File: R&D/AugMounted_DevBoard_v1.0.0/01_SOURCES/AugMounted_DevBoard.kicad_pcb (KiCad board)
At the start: 4 copper layers, 55.1 x 83.3 mm, 136 parts, among them J201 J_TYPE-C-31-M-13, J301 J_JST_S2B-PH-SM4-TB, J401 J_FH43BW-61S-0.2SHW, J501 J_0788641001_PAD, J504 J_0788641001_PAD, Q301 Q_BSS123WQ-7-F, Q302 Q_HSS2P10, Q303 Q_BSS123WQ-7-F, Q304 Q_HSS2P10, Q305 Q_BSS123WQ-7-F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

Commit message: Layout done
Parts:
- moved LOGO101 13.4 mm to (164.6, 75.9), turned to 180 degrees
- moved JP403 0.15 mm to (152.5, 114.2)
- moved JP401 0.15 mm to (157.5, 114.2)
- moved JP402 0.15 mm to (155.0, 114.2)
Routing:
- net GND: vias 104 -> 174

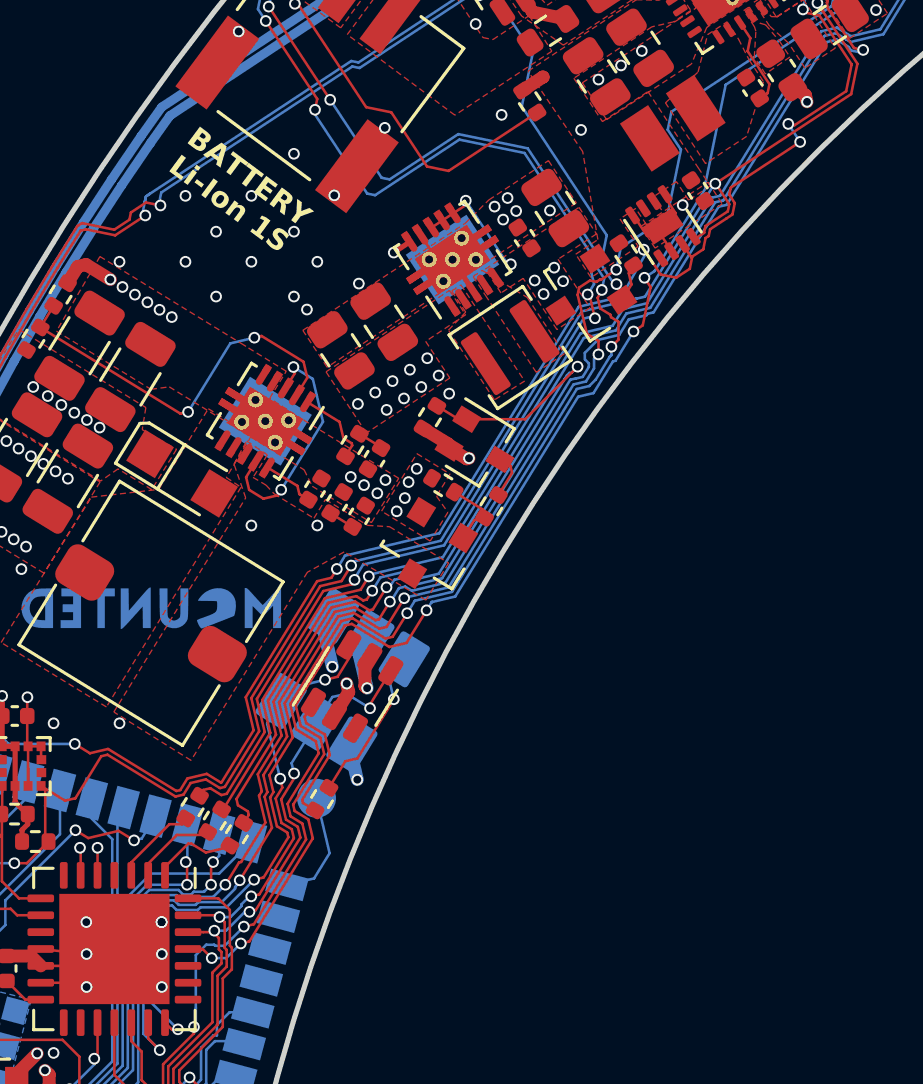
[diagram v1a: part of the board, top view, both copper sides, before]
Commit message: Excluded violations, added via stiching for GND. Ready for review/Production
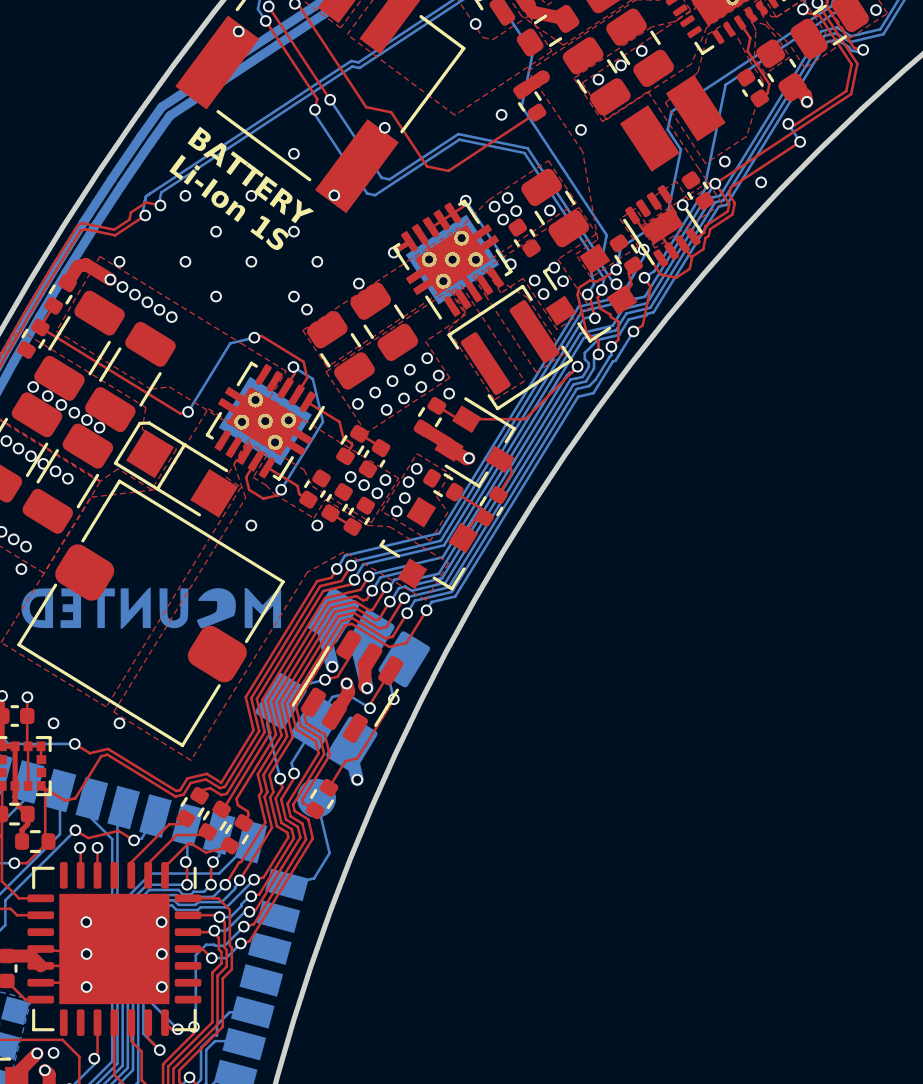
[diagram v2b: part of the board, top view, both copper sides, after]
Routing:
- net GND: vias 174 -> 175
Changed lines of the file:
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@@
           (xy 179.603773 41.320426)
           (xy 178.150624 42.694601)
-          (xy 177.326118 41.822712)
+          (xy 177.326119 41.822712)
           (xy 178.779268 40.448536)
         )
@@
           (xy 179.603773 41.320426)
           (xy 178.150624 42.694601)
-          (xy 177.326118 41.822712)
+          (xy 177.326119 41.822712)
           (xy 178.779268 40.448536)
         )
@@
   (via (at 157.160398 91.518971) (size 0.45) (drill 0.3) (layers "F.Cu" "B.Cu") (free) (net 1))
   (via (at 172.643827 63.36587) (size 0.45) (drill 0.3) (layers "F.Cu" "B.Cu") (free) (net 1))
-  (via (at 165.043827 87.96587) (size 0.45) (drill 0.3) (layers "F.Cu" "B.Cu") (net 1))
   (via (at 158.951135 108.343453) (size 0.45) (drill 0.3) (layers "F.Cu" "B.Cu") (net 1))
   (via (at 194.643827 52.86587) (size 0.45) (drill 0.3) (layers "F.Cu" "B.Cu") (free) (net 1))
@@
   (via (at 188.633169 45.090277) (size 0.45) (drill 0.3) (layers "F.Cu" "B.Cu") (net 1))
   (via (at 186.935187 43.779551) (size 0.45) (drill 0.3) (layers "F.Cu" "B.Cu") (net 1))
+  (via (at 188.143827 59.46587) (size 0.45) (drill 0.3) (layers "F.Cu" "B.Cu") (free) (net 1))
   (via (at 192.175105 52.18766) (size 0.45) (drill 0.3) (layers "F.Cu" "B.Cu") (free) (net 1))
   (via (at 162.153827 89.19587) (size 0.45) (drill 0.3) (layers "F.Cu" "B.Cu") (net 1))
@@
   (via (at 177.872524 60.399548) (size 0.45) (drill 0.3) (layers "F.Cu" "B.Cu") (free) (net 1))
   (via (at 190.643827 34.86587) (size 0.45) (drill 0.3) (layers "F.Cu" "B.Cu") (free) (net 1))
+  (via (at 186.743827 58.66587) (size 0.45) (drill 0.3) (layers "F.Cu" "B.Cu") (free) (net 1))
   (via (at 171.086099 51.449911) (size 0.45) (drill 0.3) (layers "F.Cu" "B.Cu") (free) (net 1))
   (via (at 182.643827 50.36587) (size 0.45) (drill 0.3) (layers "F.Cu" "B.Cu") (free) (net 1))
